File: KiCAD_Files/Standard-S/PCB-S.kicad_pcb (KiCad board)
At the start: 2 copper layers, 73.7 x 48.3 mm, 26 parts, among them J1 Conn_01x15_Female, J2 Conn_01x15_Female, SW1 SW_Push, SW2 SW_Push, SW3 SW_Push, U1 MCP9700AT-ETT

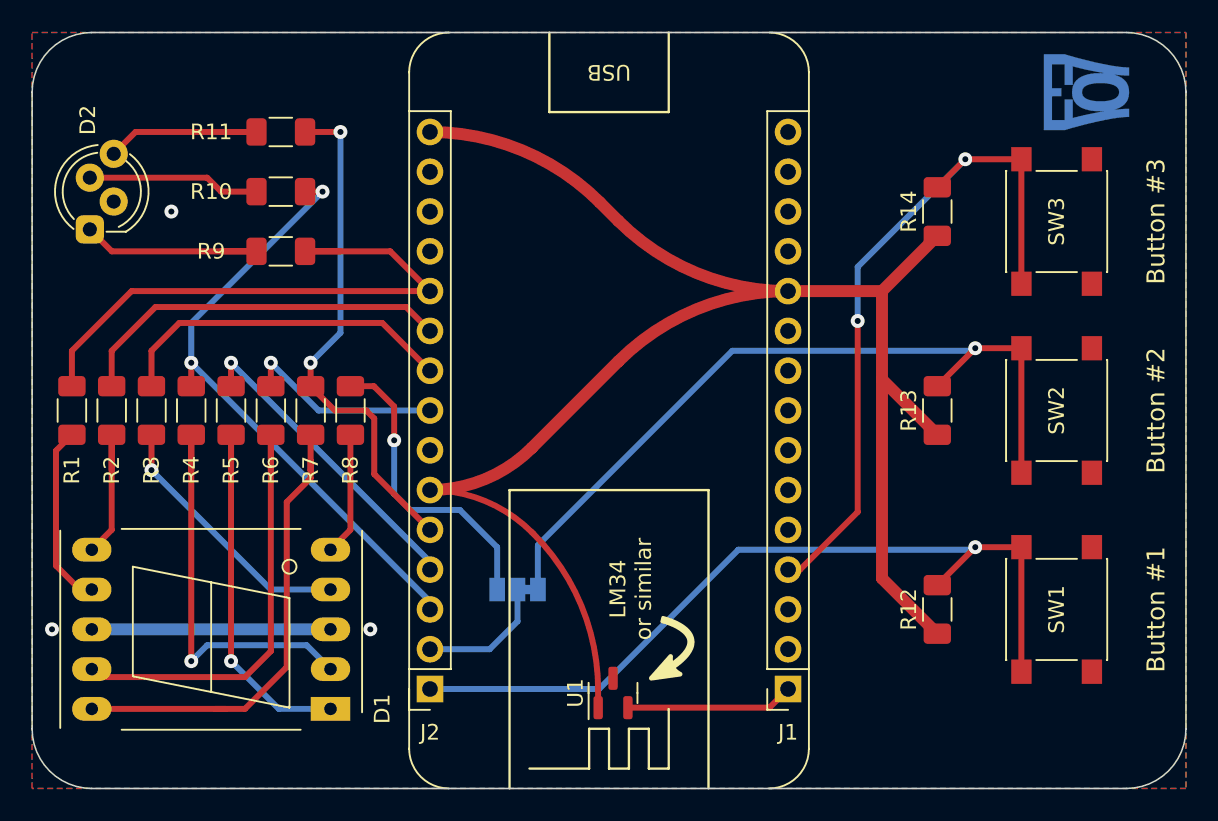
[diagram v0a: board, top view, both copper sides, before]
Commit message: Added Panelization files and stuff
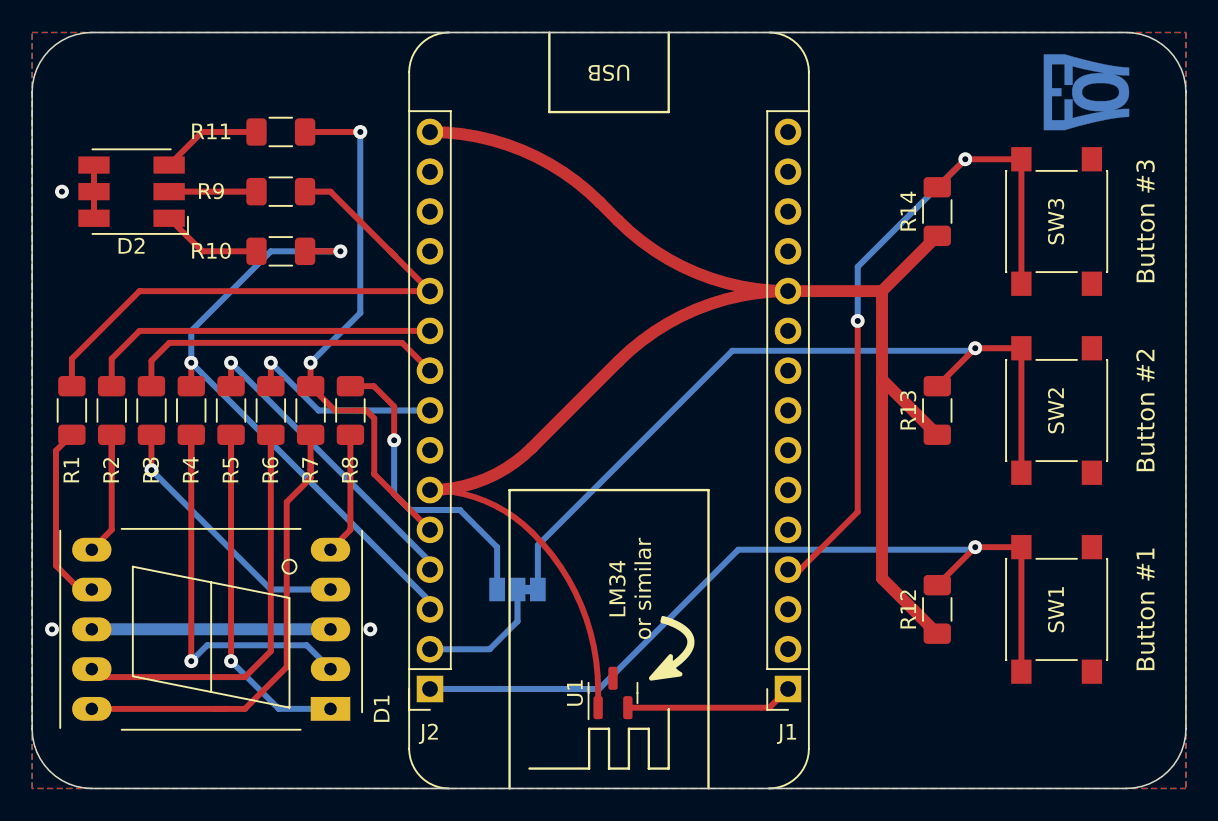
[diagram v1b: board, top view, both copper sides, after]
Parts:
- D2: value LED_RKGB -> LED_RGB; footprint LED_THT:LED_D5.0mm-4_RGB_Staggered_Pins -> LED_SMD:LED_RGB_5050-6
- moved R10 3.81 mm to (181.0, 41.3)
- moved R9 3.81 mm to (181.0, 37.5)
- moved D2 3.59 mm to (171.4, 37.5), turned to 180 degrees
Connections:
- D2 pad 2: GND -> Net-(D2-Pad2)
- D2 pad 4: Net-(D2-Pad4) -> GND
- R10 pad 2: Net-(D2-Pad3) -> Net-(D2-Pad1)
- R11 pad 2: Net-(D2-Pad4) -> Net-(D2-Pad3)
- R9 pad 2: Net-(D2-Pad1) -> Net-(D2-Pad2)
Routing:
- net Net-(D2-Pad4): track 12.0 -> 0.00 mm
- net Net-(D2-Pad1): track 13.5 -> 6.45 mm
- net Net-(D2-Pad2): track 0.00 -> 5.58 mm
- net Net-(D2-Pad3): track 11.0 -> 6.45 mm
- net GND: track 15.2 -> 18.6 mm
- net /SEGG: track 32.8 -> 34.6 mm
- net /SEGB: track 24.4 -> 22.8 mm
- net /SEGC: track 22.0 -> 20.6 mm
- net /SEGA: track 38.0 -> 37.5 mm
